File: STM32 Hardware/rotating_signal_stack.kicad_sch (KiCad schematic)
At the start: 2 parts

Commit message: Fixed the file system and continued to improve the design
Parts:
- added C1: 470 uF; 25V, symbol Device:C
- added H1, H2, H3, H4: MountingHole_Pad, symbol Mechanical:MountingHole_Pad
- added J1: Molex_Megafit_02, MRDT_Connectors:MOLEX_MegaFit_02_Horizontal, symbol MRDT_Connectors:Molex_Megafit_02
- added J3: Motor pins, Converter_DCDC:Converter_DCDC_Cyntec_MUN12AD01-SH, symbol Connector:Conn_01x04_Pin
- added R1: 10k, symbol Device:R_US
- added U3: (no value), symbol MRDT_Devices:TMAG5273
- added U4: (no value), symbol MRDT_Devices:Magnetic_Sensor
- U1: footprint (none) -> Package_QFP:LQFP-100_14x14mm_P0.5mm
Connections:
- net GND: now also C1.1, H1.1, H2.1, H3.1, H4.1, U4. (INT)
- net EN: now reaches U1.1 (EN), U2.31 (PC13)
- net M2: now reaches U1.2 (M0), U2.32 (PC14)
- net M1: now reaches U1.3 (M1), U2.33 (PC15)
- net M0: now reaches U1.4 (M2), U2.34 (PH0)
- net STEP: now reaches U1.7 (STEP), U2.39 (PA3)
- net DIR: now reaches U1.8 (DIR), U2.10 (PA10)
- net 3V3: no longer names the net of U2.3 (3V3)
- net A1: no longer names the net of U1.14 (OUTA1)
- net A1: now also J3.1 (Pin_1)
- net A2: no longer names the net of U1.13 (OUTA2)
- net A2: now also J3.2 (Pin_2)
- net B1: no longer names the net of U1.11 (OUTB1)
- net B1: now also J3.4 (Pin_4)
- net B2: no longer names the net of U1.12 (OUTB2)
- net B2: now also J3.3 (Pin_3)
- net CAN_H: no longer names the net of U2.5 (CAN_H)
- net CAN_L: no longer names the net of U2.4 (CAN_L)
- net LED1: no longer names the net of U2.24 (LED1)
- net LED2: no longer names the net of U2.23 (LED2)
- net PA0: no longer names the net of U2.38 (PA0)
- net PA15: no longer names the net of U2.9 (PA15)
- net PA4: no longer names the net of U2.40 (PA4)
- net PA6: no longer names the net of U2.41 (PA6)
- net PA8 renamed INT
- net INT: now also U4. (INT)
- net PA9: no longer names the net of U2.11 (PA9)
- net PB0: no longer names the net of U2.42 (PB0)
- net PB1: no longer names the net of U2.43 (PB1)
- net PB10: no longer names the net of U2.45 (PB10)
- net PB13 renamed nSTBY
- net nSTBY: now also U1.6 (nSTBY), R1.1
- net PB14: no longer names the net of U2.17 (PB14)
- net PB2: no longer names the net of U2.44 (PB2)
- net PB4: no longer names the net of U2.26 (PB4)
- net PB5: no longer names the net of U2.27 (PB5)
- net PB6: no longer names the net of U2.28 (PB6)
- net PB7 renamed SCL
- net SCL: now also U4. (INT)
- net PB8 renamed SDA
- net SDA: now also U4. (INT)
- net PC10: no longer names the net of U2.8 (PC10)
- net PC11: no longer names the net of U2.7 (PC11)
- net PC12: no longer names the net of U2.6 (PC12)
- net PC2: no longer names the net of U2.36 (PC2)
- net PC3: no longer names the net of U2.37 (PC3)
- net PC6: no longer names the net of U2.16 (PC6)
- net PC7: no longer names the net of U2.15 (PC7)
- net PC8: no longer names the net of U2.14 (PC8)
- net PC9: no longer names the net of U2.13 (PC9)
- net PD2: no longer names the net of U2.25 (PD2)
- net PH1: no longer names the net of U2.35 (PH1)
- net RX+: no longer names the net of U2.19 (RX+)
- net RX-: no longer names the net of U2.20 (RX-)
- net TX+: no longer names the net of U2.21 (TX+)
- net TX-: no longer names the net of U2.22 (TX-)
- net VCC 24V renamed +12V
- net +12V: now also C1.2
- net VCC 3V3 renamed +3V3
- net +3V3: now also R1.2, U4. (INT); no longer U1.6 (nSTBY)
- no-connect marks 1 -> 34
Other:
- moved on the sheet: U2

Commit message: Improved formating and added LED indicators, test buttons, and power inputs
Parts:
- added D1: LED, LED_SMD:LED_0603_1608Metric_Pad1.05x0.95mm_HandSolder, symbol Device:LED
- added SW1, SW2: SW_Push, Button_Switch_THT:SW_NKK_GW12LJP, symbol Switch:SW_Push
- C1: footprint (none) -> Capacitor_SMD:C_0603_1608Metric_Pad1.08x0.95mm_HandSolder
- H1, H2, H3, H4: footprint (none) -> MRDT_Drill_Holes:4_40_Hole_Pad_Via
- R1: footprint (none) -> Resistor_SMD:R_0201_0603Metric_Pad0.64x0.40mm_HandSolder
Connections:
- net +12V is gone; now on net 12V: C1.2, U1.9 (VM), U2.1 (VIN)
- net +3V3: no longer U4. (INT)
- net GND: now also D1.1 (K)
- net 3V3: now reaches U2.3 (3V3)
- net 3V3: now also U4. (INT)
- net 12V: now reaches J1.1
- net 12V: now also J1.2, D1.2 (A)
- no-connect marks 34 -> 33
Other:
- moved on the sheet: C1, J3, R1, U1, U4

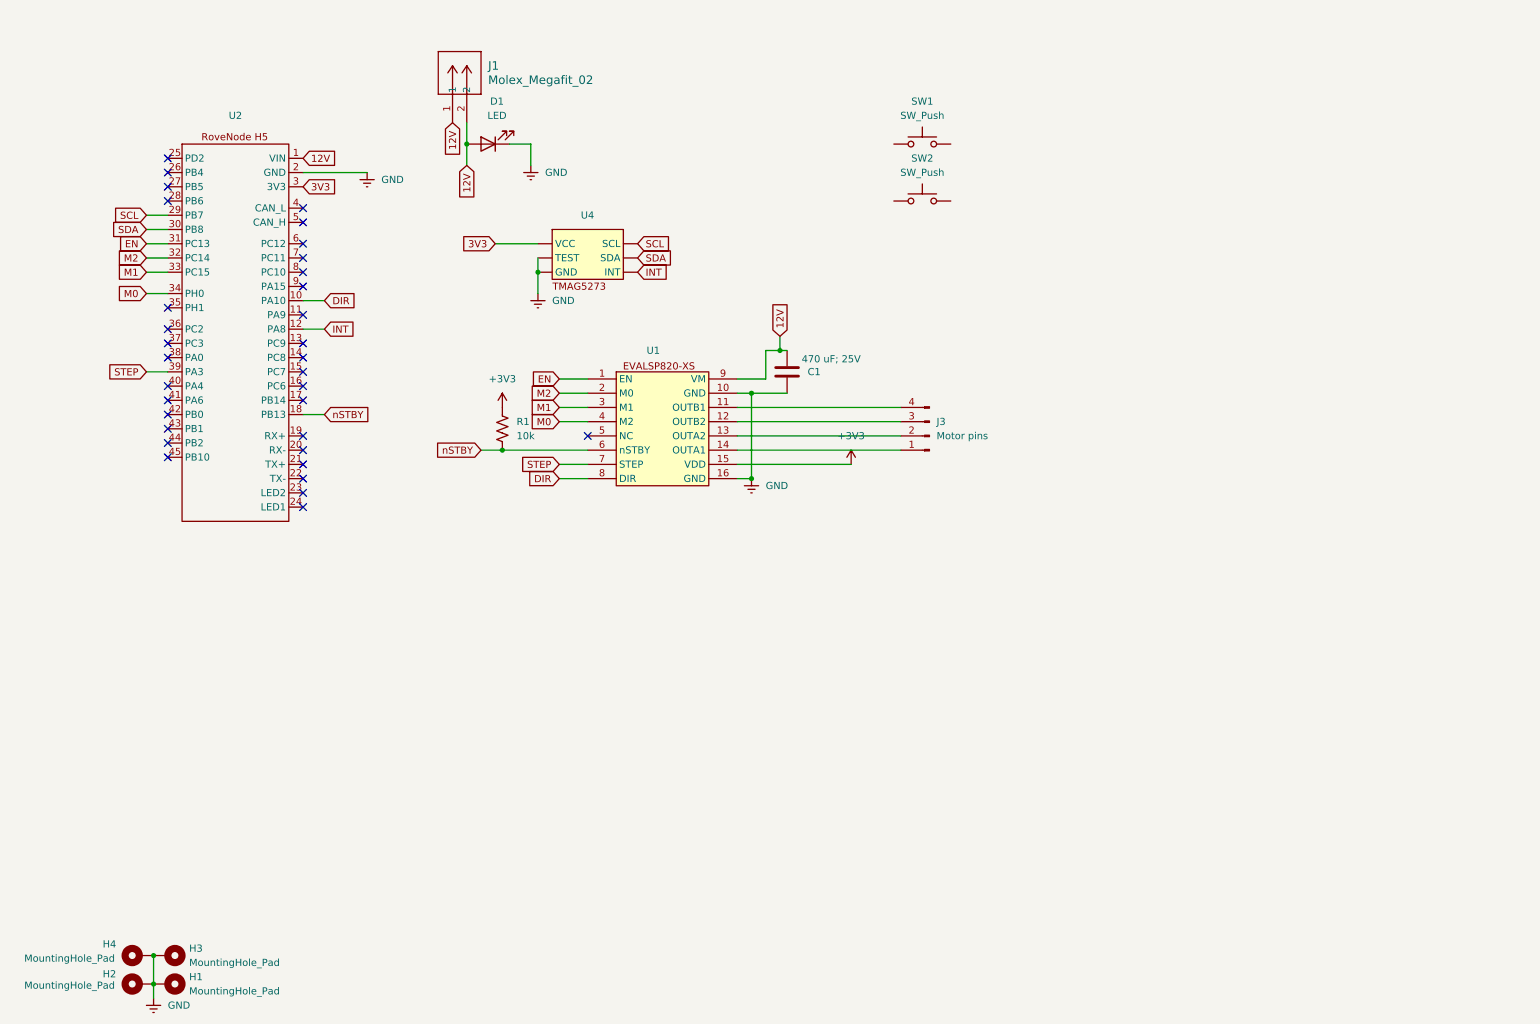
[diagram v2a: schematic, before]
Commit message: Added ethernet connector
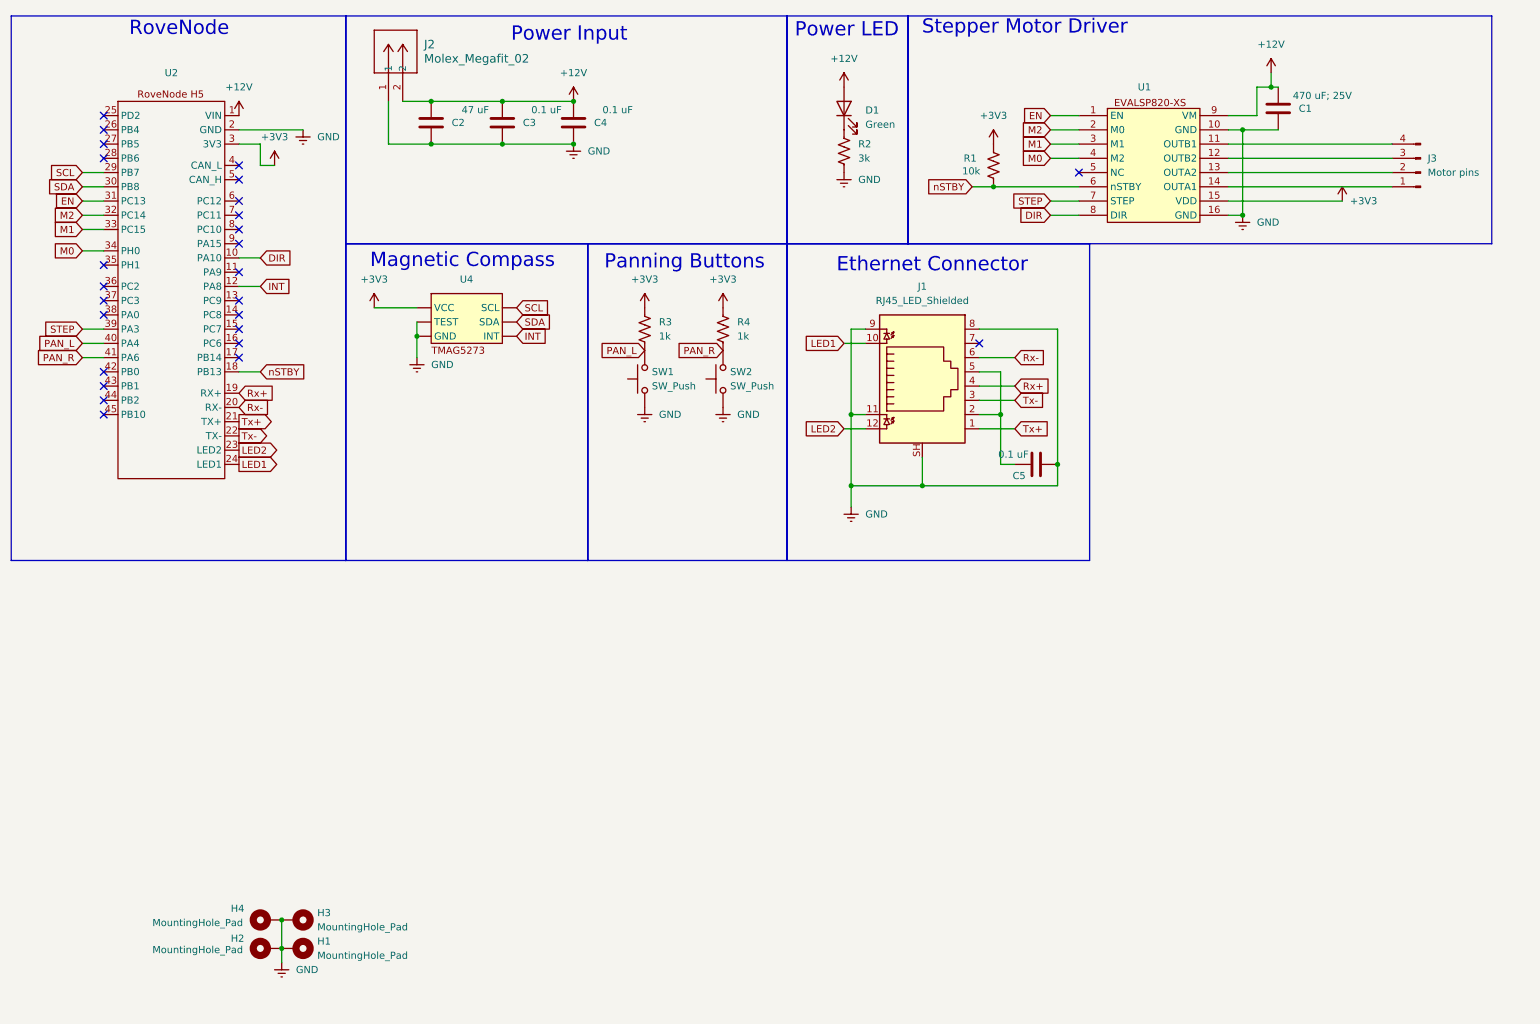
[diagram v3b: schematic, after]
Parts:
- removed J1: Molex_Megafit_02, MRDT_Connectors:MOLEX_MegaFit_02_Horizontal, symbol MRDT_Connectors:Molex_Megafit_02
- added C2: 47 uF, Capacitor_SMD:C_0603_1608Metric_Pad1.08x0.95mm_HandSolder, symbol Device:C
- added C3, C4, C5: 0.1 uF, Capacitor_SMD:C_0603_1608Metric_Pad1.08x0.95mm_HandSolder, symbol Device:C
- added J1: RJ45_LED_Shielded, symbol Connector:RJ45_LED_Shielded
- added J2: Molex_Megafit_02, MRDT_Connectors:MOLEX_MegaFit_02_Horizontal, symbol MRDT_Connectors:Molex_Megafit_02
- added R2: 3k, Resistor_SMD:R_0201_0603Metric_Pad0.64x0.40mm_HandSolder, symbol Device:R_US
- added R3, R4: 1k, Resistor_SMD:R_0201_0603Metric_Pad0.64x0.40mm_HandSolder, symbol Device:R_US
- D1: value LED -> Green
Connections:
- net +3V3: now also U2.3 (3V3), U4. (INT), R3.2, R4.2
- net GND: now also SW1.1, SW2.1, C2.1, C3.1, C4.1, C5.1, J1.11, J1.8, J1.9, J1.SH, J2.1, R2.1; no longer D1.1 (K)
- net PAN_L: now reaches SW1.2
- net PAN_L: now also U2.40 (PA4), R3.1
- net Rx+: now reaches U2.19 (RX+)
- net Rx+: now also J1.4
- net Rx-: now reaches U2.20 (RX-)
- net Rx-: now also J1.6
- net Tx+: now reaches U2.21 (TX+)
- net Tx+: now also J1.1
- net Tx-: now reaches U2.22 (TX-)
- net Tx-: now also J1.3
- net LED2: now reaches U2.23 (LED2)
- net LED2: now also J1.12
- net LED1: now reaches U2.24 (LED1)
- net LED1: now also J1.10
- net PAN_R: now reaches U2.41 (PA6)
- net PAN_R: now also SW2.2, R4.1
- net 12V renamed +12V
- net +12V: now also C2.2, C3.2, C4.2, J2.2
- removed net 3V3: U2.3 (3V3), U4. (INT)
- new net: D1.1 (K), R2.2
- new net: C5.2, J1.2, J1.5
- no-connect marks 33 -> 26
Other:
- note added: "Ethernet Connector"
- note added: "Magnetic Compass"
- note added: "Panning Buttons"
- note added: "Power Input"
- note added: "Power LED"
- note added: "RoveNode"
- note added: "Stepper Motor Driver"
- moved on the sheet: C1, D1, H1, H2, H3, H4, J3, R1, SW1, SW2, U1, U2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

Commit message: Added Reverse Voltage Protection
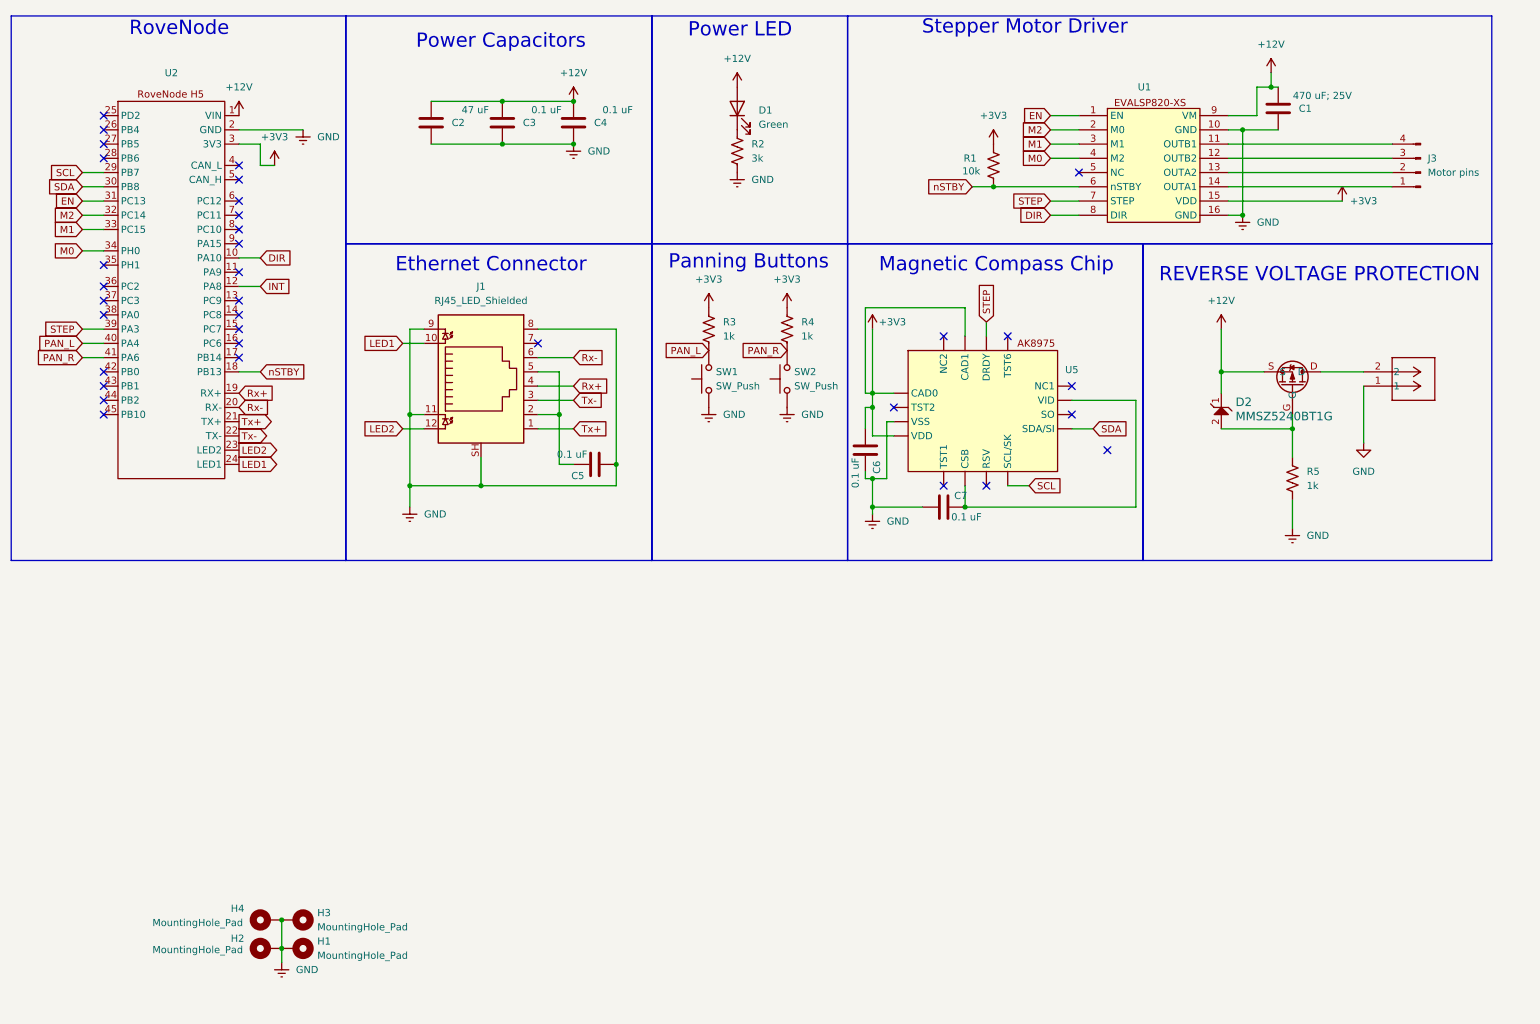
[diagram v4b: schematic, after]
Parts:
- removed J2: Molex_Megafit_02, MRDT_Connectors:MOLEX_MegaFit_02_Horizontal, symbol MRDT_Connectors:Molex_Megafit_02
- removed U4: (no value), symbol MRDT_Devices:Magnetic_Sensor
- added C6, C7: 0.1 uF, Capacitor_SMD:C_0603_1608Metric_Pad1.08x0.95mm_HandSolder, symbol Device:C
- added D2: MMSZ5240BT1G, MRDT_Devices:SOD-123_ONS-L, symbol MRDT_Devices:MMSZ5240BT1G
- added J4: Molex_Megafit_02, MRDT_Connectors:MOLEX_MegaFit_02_Horizontal, symbol MRDT_Connectors:Molex_Megafit_02
- added Q1: TPC8132_LQS, MRDT_Devices:TPC8132_LQS, symbol MRDT_Devices:TPC8132_LQS
- added R5: 1k, Package_DIP:DIP-8_W7.62mm, symbol Device:R_US
- added U5: (no value), symbol RotatingSignalStack_Symbol:AKM8975
- U1: footprint Package_QFP:LQFP-100_14x14mm_P0.5mm -> RotatingSignalStack_Footprints:EVALSP820-XS
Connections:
- net +12V: now also D2.1, Q1.S
- net +3V3: now also C6.1, U5. (SDA/SI)
- net GND: now also C6.2, C7.1, J4.1, R5.2, U5. (SDA/SI)
- net SCL: now also U5. (SDA/SI)
- net SDA: now also U5. (SDA/SI)
- net STEP: now also U5. (SDA/SI)
- new net: C7.2, U5. (SDA/SI)
- new net: D2.2, Q1.G, R5.1
- new net: J4.2, Q1.D
- no-connect marks 26 -> 34
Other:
- note added: "Magnetic Compass Chip"
- note added: "Power Capacitors"
- note added: "REVERSE VOLTAGE PROTECTION"
- note removed: "Magnetic Compass"
- note removed: "Power Input"
- moved on the sheet: C5, D1, J1, R2, R3, R4, SW1, SW2

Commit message: Assigned footprints to all symbols besides the compass
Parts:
- J1: footprint (none) -> Connector_RJ:RJ45_Abracon_ARJP11A-MA_Horizontal
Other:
- moved on the sheet: R3, R4, SW1, SW2

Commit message: Added PCB layout
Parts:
- removed C6, C7: 0.1 uF, Capacitor_SMD:C_0603_1608Metric_Pad1.08x0.95mm_HandSolder, symbol Device:C
- removed U5: (no value), symbol RotatingSignalStack_Symbol:AKM8975
- J3: footprint Converter_DCDC:Converter_DCDC_Cyntec_MUN12AD01-SH -> Connector:NS-Tech_Grove_1x04_P2mm_Vertical
- R5: footprint Package_DIP:DIP-8_W7.62mm -> Resistor_SMD:R_0201_0603Metric_Pad0.64x0.40mm_HandSolder
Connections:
- no-connect marks 34 -> 26
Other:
- note removed: "Magnetic Compass Chip"
